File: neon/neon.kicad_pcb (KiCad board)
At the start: 2 copper layers, 60 x 50 mm, 46 parts, among them J1 V3V3-VIO, J2 V3V3-GND, J3 V3V3-GND, J4 V3V3-GND, J5 VBUS-VCC, Q1 BC807, Q2 BC807, Q3 BC807, Q4 BC807, Q5 BC807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

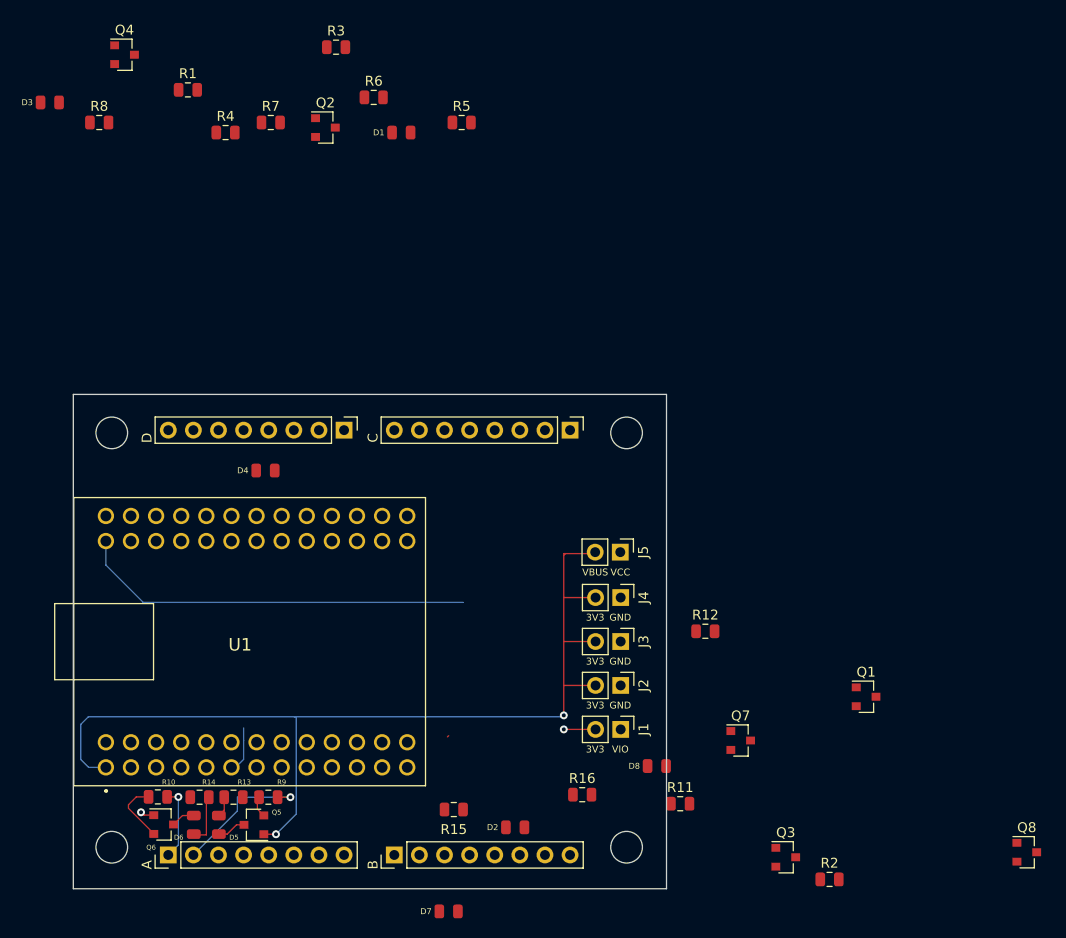
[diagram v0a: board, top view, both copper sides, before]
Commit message: Version with shift register - schematic
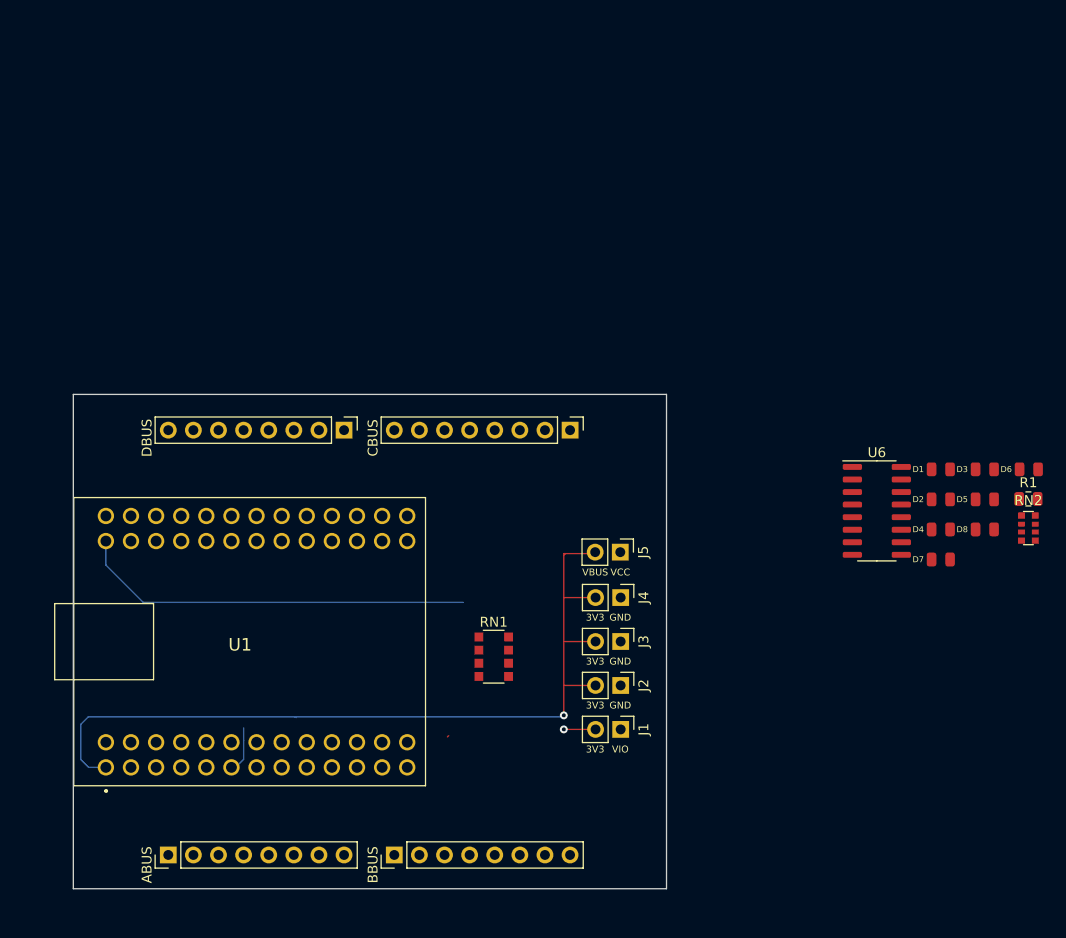
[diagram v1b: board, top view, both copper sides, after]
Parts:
- removed Q1, Q2, Q3, Q4, Q5, Q6, Q7, Q8: BC807, Package_TO_SOT_SMD:SOT-23
- removed R10, R11, R12, R5, R6, R7, R8, R9: 10k, Resistor_SMD:R_0805_2012Metric
- removed R13, R14, R15, R16, R2, R3, R4: 330, Resistor_SMD:R_0805_2012Metric
- removed REF** (x4): MountingHole_3.2mm_M3, MountingHole:MountingHole_3.2mm_M3
- added RN1: 330, Resistor_SMD:R_Array_Convex_4x1206, F.Cu at (158.0, 106.5)
- added RN2: 330, Resistor_SMD:R_Array_Convex_4x0612, F.Cu at (212.1, 93.5)
- added U6: 74HC595, Package_SO:SOIC-16_3.9x9.9mm_P1.27mm, F.Cu at (196.8, 91.7)
- R1: value 330 -> 10k
- U2: value A -> ABUS
- U3: value B -> BBUS
- U4: value C -> CBUS
- U5: value D -> DBUS
- moved D3 101.6 mm to (207.7, 87.5)
- moved R1 94.5 mm to (212.1, 90.5)
- moved D6 91.8 mm to (212.1, 87.5), turned to 0 degrees
- moved D5 84.2 mm to (207.7, 90.5), turned to 0 degrees
- moved D4 68.6 mm to (203.2, 93.6)
- moved D1 64.3 mm to (203.2, 87.5)
- moved D7 61.2 mm to (203.2, 96.6)
- moved D2 54.3 mm to (203.2, 90.5)
- moved D8 40.9 mm to (207.7, 93.6)
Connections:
- D1 pad 1: Net-(D1-Pad1) -> GND
- D2 pad 1: Net-(D2-Pad1) -> GND
- D3 pad 1: Net-(D3-Pad1) -> GND
- D4 pad 1: Net-(D4-Pad1) -> GND
- D5 pad 1: Net-(D5-Pad1) -> GND
- D6 pad 1: Net-(D6-Pad1) -> GND
- D7 pad 1: Net-(D7-Pad1) -> GND
- D8 pad 1: Net-(D8-Pad1) -> GND
- R1 pad 1: Net-(D1-Pad1) -> /FT4232H.sch/PWREN
- R1 pad 2: GND -> /FT4232H.sch/VIO
- U1 pad 29: Net-(U1-Pad29) -> /FT4232H.sch/CS
- U1 pad 30: Net-(U1-Pad30) -> /FT4232H.sch/DATA
- U1 pad 42: Net-(U1-Pad42) -> /FT4232H.sch/CLK
- U1 pad 43: Net-(U1-Pad43) -> /FT4232H.sch/PWREN
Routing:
- net V3V3: track 100.2 -> 84.9 mm, vias 4 -> 2
- net /FT4232H.sch/AD1: track 14.4 -> 0.00 mm, vias 1 -> 0
- net /FT4232H.sch/AD0: track 7.44 -> 0.00 mm, vias 1 -> 0
- net Net-(Q6-Pad2): track 6.60 -> 0.00 mm
- net Net-(D6-Pad1): track 5.16 -> 0.00 mm
- net Net-(D5-Pad2): track 3.04 -> 0.00 mm
- net Net-(D6-Pad2): track 2.42 -> 0.00 mm
- net Net-(D5-Pad1): track 2.19 -> 0.00 mm
- net Net-(Q5-Pad2): track 2.11 -> 0.00 mm

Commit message: Assign LEDs on pcb
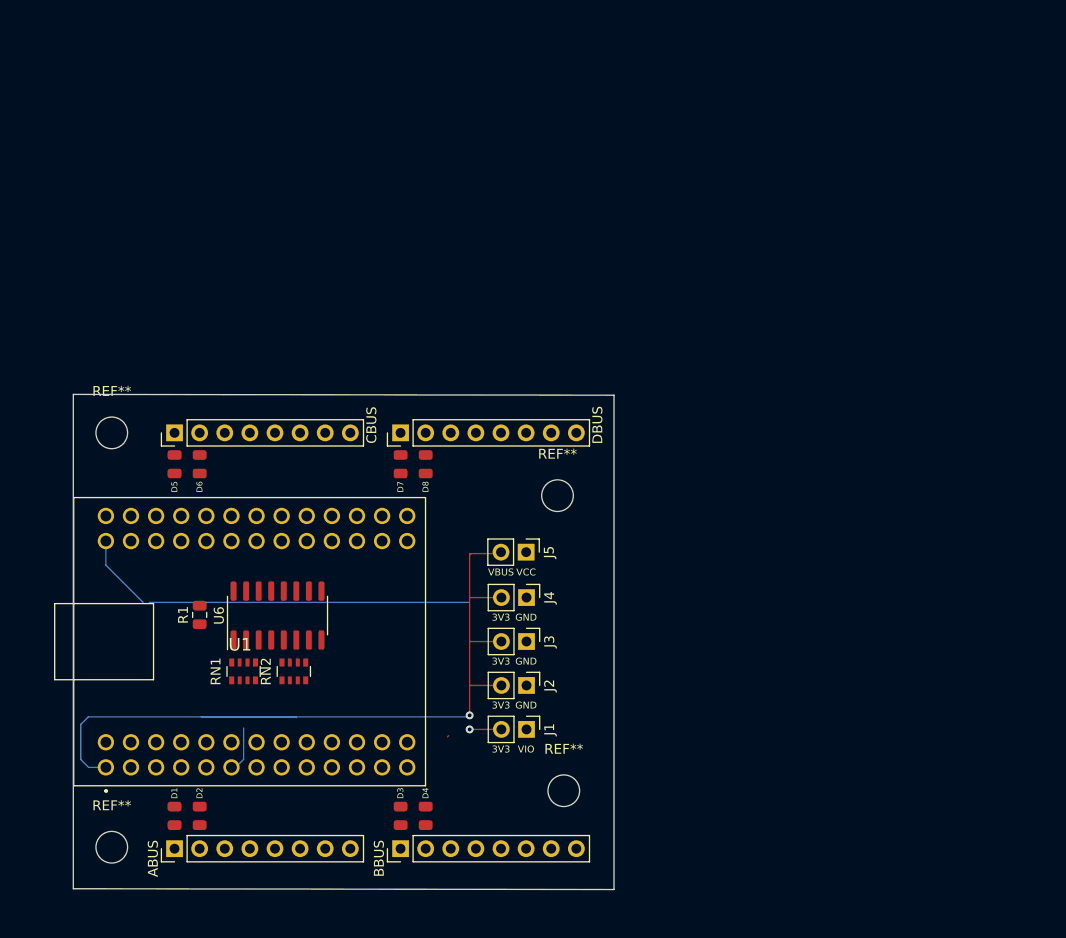
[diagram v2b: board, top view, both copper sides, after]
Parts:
- added REF**: MountingHole_3.2mm_M3, MountingHole:MountingHole_3.2mm_M3, F.Cu at (165.1, 120.0)
- added REF**: MountingHole_3.2mm_M3, MountingHole:MountingHole_3.2mm_M3, F.Cu at (164.5, 90.2)
- added REF**: MountingHole_3.2mm_M3, MountingHole:MountingHole_3.2mm_M3, F.Cu at (119.4, 125.7)
- added REF**: MountingHole_3.2mm_M3, MountingHole:MountingHole_3.2mm_M3, F.Cu at (119.4, 83.8)
- RN1: footprint Resistor_SMD:R_Array_Convex_4x1206 -> Resistor_SMD:R_Array_Convex_4x0603
- RN2: footprint Resistor_SMD:R_Array_Convex_4x0612 -> Resistor_SMD:R_Array_Convex_4x0603
- moved D1 85.1 mm to (125.7, 122.6), turned to 270 degrees
- moved R1 84.6 mm to (128.3, 102.2), turned to 90 degrees
- moved D6 83.9 mm to (128.3, 87.0), turned to 90 degrees
- moved D5 82.0 mm to (125.7, 87.0), turned to 90 degrees
- moved D2 81.5 mm to (128.3, 122.6), turned to 270 degrees
- moved RN2 75.7 mm to (137.8, 108.0), turned to 90 degrees
- moved D3 68.7 mm to (148.6, 122.6), turned to 270 degrees
- moved U6 61.5 mm to (136.1, 102.3), turned to 90 degrees
- moved D4 59.6 mm to (151.1, 122.6), turned to 270 degrees
- moved D8 56.9 mm to (151.1, 87.0), turned to 90 degrees
- moved D7 55.5 mm to (148.6, 87.0), turned to 90 degrees
- moved U4 40.0 mm to (125.7, 83.8), turned to 90 degrees
- moved RN1 25.3 mm to (132.7, 108.0), turned to 90 degrees
- moved J1 9.53 mm to (161.3, 113.8)
- moved J2 9.53 mm to (161.3, 109.4)
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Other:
- board size 60 x 50 mm -> 54.7 x 50.1 mm

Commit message: A BUS
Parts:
- turned D1 to 90 degrees
- turned D2 to 90 degrees
- turned D3 to 90 degrees
- turned D4 to 90 degrees
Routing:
- net /FT4232H.sch/VBUS: track 43.5 -> 0.18 mm
- net Net-(D2-Pad2): track 0.00 -> 34.4 mm
- net Net-(D1-Pad2): track 0.00 -> 33.0 mm
- net Net-(D3-Pad2): track 0.00 -> 30.9 mm
- net Net-(D4-Pad2): track 0.00 -> 29.2 mm
- net Net-(RN1-Pad8): track 0.00 -> 18.4 mm, vias 0 -> 2
- net /FT4232H.sch/AD6: track 0.00 -> 13.7 mm
- net /FT4232H.sch/AD4: track 0.00 -> 12.6 mm
- net /FT4232H.sch/AD3: track 0.00 -> 12.6 mm
- net /FT4232H.sch/AD7: track 0.00 -> 11.9 mm
- net /FT4232H.sch/AD1: track 0.00 -> 11.8 mm
- net /FT4232H.sch/AD5: track 0.00 -> 10.0 mm
- net /FT4232H.sch/AD2: track 0.00 -> 9.00 mm
- net /FT4232H.sch/AD0: track 0.00 -> 8.50 mm
- net GND: track 0.00 -> 4.62 mm, vias 0 -> 1
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
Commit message: Texts ideas
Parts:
- U2: value ABUS -> A; footprint Connector_PinHeader_2.54mm:PinHeader_1x08_P2.54mm_Vertical -> neon_footprints:PinHeader_1x08_P2.54mm_Vertical
- U3: value BBUS -> B; footprint Connector_PinHeader_2.54mm:PinHeader_1x08_P2.54mm_Vertical -> neon_footprints:PinHeader_1x08_P2.54mm_Vertical
- U4, U5: footprint Connector_PinHeader_2.54mm:PinHeader_1x08_P2.54mm_Vertical -> neon_footprints:PinHeader_1x08_P2.54mm_Vertical
- moved D4 1.28 mm to (151.7, 121.4), turned to 0 degrees
- moved D3 1.18 mm to (148.3, 121.4), turned to 180 degrees
- moved D1 0.51 mm to (125.7, 122.0)
- moved D2 0.51 mm to (128.3, 122.0)
- moved U2 0.51 mm to (125.7, 125.4)
- moved U3 0.51 mm to (148.6, 125.4)
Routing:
- net Net-(D4-Pad2): track 29.2 -> 21.4 mm
- net GND: track 4.62 -> 12.4 mm
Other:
- board size 54.7 x 50.1 mm -> 54.7 x 50 mm
- board text added: "0"
- board text added: "1"
- board text added: "2"
- board text added: "3"
- board text added: "CS"
- board text added: "CTS"
- board text added: "DCD"
- board text added: "DSR"
- board text added: "DTR"
- board text added: "GPIO"
- board text added: "MISO"
- board text added: "MOSI"
- board text added: "RI"
- board text added: "RTS"
- board text added: "RX"
- board text added: "SCK"
- board text added: "TCK"
- board text added: "TDI"
- board text added: "TDO"
- board text added: "TMS"
- board text added: "TX"

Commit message: More labels
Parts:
- U5: value DBUS -> D
- moved D7 1.27 mm to (148.6, 88.3)
- moved D8 1.27 mm to (151.1, 88.3)
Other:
- board text added: "4"
- board text added: "5"
- board text added: "6"
- board text added: "7"
- board text added: "GPIO0"
- board text added: "GPIO1"
- board text added: "GPIO2"
- board text added: "GPIO3"
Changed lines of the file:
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@@
   (general
     (thickness 1.6)
-    (drawings 65)
+    (drawings 121)
     (tracks 109)
     (zones 0)
@@
       (effects (font (size 1 1) (thickness 0.15)))
     )
-    (fp_text value DBUS (at -0.1054 -2.159 90) (layer F.SilkS)
-      (effects (font (size 1 1) (thickness 0.15)))
-    )
-    (fp_text user %R (at -1.175 9.634 180) (layer F.Fab)
+    (fp_text value D (at -0.1054 -2.159 90) (layer F.SilkS)
+      (effects (font (size 1 1) (thickness 0.15)))
+    )
+    (fp_text user %R (at 0 19.812 180) (layer F.Fab)
       (effects (font (size 1 1) (thickness 0.15)))
     )
@@
   )
   (module neon_footprints:LED_0805_2012Metric (layer F.Cu)
-    (at 151.13 86.995 90)
+    (at 151.13 88.265 90)
     (descr "LED SMD 0805 (2012 Metric), square (rectangular) end terminal, IPC_7351 nominal, (Body size source: https://docs.google.com/spreadsheets/d/1BsfQQcO9C6DZCsRaXUlFlo91Tg2WpOkGARC1WS5S8t0/edit?usp=sharing), generated with kicad-footprint-generator")
     (tags diode)
@@
   )
   (module neon_footprints:LED_0805_2012Metric (layer F.Cu)
-    (at 148.59 86.995 90)
+    (at 148.59 88.265 90)
     (descr "LED SMD 0805 (2012 Metric), square (rectangular) end terminal, IPC_7351 nominal, (Body size source: https://docs.google.com/spreadsheets/d/1BsfQQcO9C6DZCsRaXUlFlo91Tg2WpOkGARC1WS5S8t0/edit?usp=sharing), generated with kicad-footprint-generator")
     (tags diode)
@@
     )
   )
+  (gr_text TMS (at 132.842 79.756 90) (layer F.SilkS)
+    (effects (font (size 0.7112 0.7112) (thickness 0.175)) (justify left))
+  )
+  (gr_text TDO (at 130.302 79.756 90) (layer F.SilkS)
+    (effects (font (size 0.7112 0.7112) (thickness 0.175)) (justify left))
+  )
+  (gr_text GPIO1 (at 138.938 82.296 90) (layer F.SilkS)
+    (effects (font (size 0.7112 0.7112) (thickness 0.175)) (justify left))
+  )
+  (gr_text GPIO2 (at 141.478 82.296 90) (layer F.SilkS)
+    (effects (font (size 0.7112 0.7112) (thickness 0.175)) (justify left))
+  )
+  (gr_text TDI (at 127.762 79.756 90) (layer F.SilkS)
+    (effects (font (size 0.7112 0.7112) (thickness 0.175)) (justify left))
+  )
+  (gr_text "GPIO3\n" (at 144.018 82.296 90) (layer F.SilkS)
+    (effects (font (size 0.7112 0.7112) (thickness 0.175)) (justify left))
+  )
+  (gr_text MISO (at 131.318 79.756 90) (layer F.SilkS)
+    (effects (font (size 0.7112 0.7112) (thickness 0.175)) (justify left))
+  )
+  (gr_text CS (at 133.858 79.756 90) (layer F.SilkS)
+    (effects (font (size 0.7112 0.7112) (thickness 0.175)) (justify left))
+  )
+  (gr_text TCK (at 125.222 79.756 90) (layer F.SilkS)
+    (effects (font (size 0.7112 0.7112) (thickness 0.175)) (justify left))
+  )
+  (gr_text MOSI (at 128.778 79.756 90) (layer F.SilkS)
+    (effects (font (size 0.7112 0.7112) (thickness 0.175)) (justify left))
+  )
+  (gr_text SCK (at 126.238 79.756 90) (layer F.SilkS)
+    (effects (font (size 0.7112 0.7112) (thickness 0.175)) (justify left))
+  )
+  (gr_text RI (at 143.002 82.296 90) (layer F.SilkS)
+    (effects (font (size 0.7112 0.7112) (thickness 0.175)) (justify left))
+  )
+  (gr_text GPIO0 (at 136.398 82.296 90) (layer F.SilkS)
+    (effects (font (size 0.7112 0.7112) (thickness 0.175)) (justify left))
+  )
+  (gr_text 4 (at 135.89 85.09 90) (layer F.SilkS)
+    (effects (font (size 0.9144 0.9144) (thickness 0.175)) (justify right))
+  )
+  (gr_text 3 (at 133.35 85.09 90) (layer F.SilkS)
+    (effects (font (size 0.9144 0.9144) (thickness 0.175)) (justify right))
+  )
+  (gr_text 2 (at 130.81 85.09 90) (layer F.SilkS)
+    (effects (font (size 0.9144 0.9144) (thickness 0.175)) (justify right))
+  )
+  (gr_text 0 (at 125.73 85.09 90) (layer F.SilkS)
+    (effects (font (size 0.9144 0.9144) (thickness 0.175)) (justify right))
+  )
+  (gr_text RX (at 128.27 82.296 90) (layer F.SilkS)
+    (effects (font (size 0.8128 0.8128) (thickness 0.175)) (justify left))
+  )
+  (gr_text 6 (at 140.97 85.09 90) (layer F.SilkS)
+    (effects (font (size 0.9144 0.9144) (thickness 0.175)) (justify right))
+  )
+  (gr_text 7 (at 143.51 85.09 90) (layer F.SilkS)
+    (effects (font (size 0.9144 0.9144) (thickness 0.175)) (justify right))
+  )
+  (gr_text 1 (at 128.27 85.09 90) (layer F.SilkS)
+    (effects (font (size 0.9144 0.9144) (thickness 0.175)) (justify right))
+  )
+  (gr_text 5 (at 138.43 85.09 90) (layer F.SilkS)
+    (effects (font (size 0.9144 0.9144) (thickness 0.175)) (justify right))
+  )
+  (gr_text DCD (at 140.462 82.296 90) (layer F.SilkS)
+    (effects (font (size 0.7112 0.7112) (thickness 0.175)) (justify left))
+  )
+  (gr_text TX (at 125.73 82.296 90) (layer F.SilkS)
+    (effects (font (size 0.8128 0.8128) (thickness 0.175)) (justify left))
+  )
+  (gr_text RTS (at 130.81 82.296 90) (layer F.SilkS)
+    (effects (font (size 0.8128 0.8128) (thickness 0.175)) (justify left))
+  )
+  (gr_text DSR (at 137.922 82.296 90) (layer F.SilkS)
+    (effects (font (size 0.7112 0.7112) (thickness 0.175)) (justify left))
+  )
+  (gr_text "CTS\n" (at 133.35 82.296 90) (layer F.SilkS)
+    (effects (font (size 0.8128 0.8128) (thickness 0.175)) (justify left))
+  )
+  (gr_text DTR (at 135.382 82.296 90) (layer F.SilkS)
+    (effects (font (size 0.7112 0.7112) (thickness 0.175)) (justify left))
+  )
+  (gr_text CS (at 156.21 77.216 90) (layer F.SilkS)
+    (effects (font (size 0.7112 0.7112) (thickness 0.175)) (justify left))
+  )
+  (gr_text MISO (at 153.67 77.216 90) (layer F.SilkS)
+    (effects (font (size 0.7112 0.7112) (thickness 0.175)) (justify left))
+  )
+  (gr_text MOSI (at 151.13 77.216 90) (layer F.SilkS)
+    (effects (font (size 0.7112 0.7112) (thickness 0.175)) (justify left))
+  )
+  (gr_text SCK (at 148.59 77.216 90) (layer F.SilkS)
+    (effects (font (size 0.7112 0.7112) (thickness 0.175)) (justify left))
+  )
+  (gr_text "GPIO3\n" (at 166.37 79.756 90) (layer F.SilkS)
+    (effects (font (size 0.7112 0.7112) (thickness 0.175)) (justify left))
+  )
+  (gr_text TDI (at 151.13 79.756 90) (layer F.SilkS)
+    (effects (font (size 0.7112 0.7112) (thickness 0.175)) (justify left))
+  )
+  (gr_text GPIO2 (at 163.83 79.756 90) (layer F.SilkS)
+    (effects (font (size 0.7112 0.7112) (thickness 0.175)) (justify left))
+  )
+  (gr_text TCK (at 148.59 79.756 90) (layer F.SilkS)
+    (effects (font (size 0.7112 0.7112) (thickness 0.175)) (justify left))
+  )
+  (gr_text TDO (at 153.67 79.756 90) (layer F.SilkS)
+    (effects (font (size 0.7112 0.7112) (thickness 0.175)) (justify left))
+  )
+  (gr_text GPIO1 (at 161.29 79.756 90) (layer F.SilkS)
+    (effects (font (size 0.7112 0.7112) (thickness 0.175)) (justify left))
+  )
+  (gr_text TMS (at 156.21 79.756 90) (layer F.SilkS)
+    (effects (font (size 0.7112 0.7112) (thickness 0.175)) (justify left))
+  )
+  (gr_text GPIO0 (at 158.75 79.756 90) (layer F.SilkS)
+    (effects (font (size 0.7112 0.7112) (thickness 0.175)) (justify left))
+  )
+  (gr_text 7 (at 166.37 85.09 90) (layer F.SilkS)
+    (effects (font (size 0.7112 0.7112) (thickness 0.175)) (justify right))
+  )
+  (gr_text 6 (at 163.83 85.09 90) (layer F.SilkS)
+    (effects (font (size 0.7112 0.7112) (thickness 0.175)) (justify right))
+  )
+  (gr_text 5 (at 161.29 85.09 90) (layer F.SilkS)
+    (effects (font (size 0.7112 0.7112) (thickness 0.175)) (justify right))
+  )
+  (gr_text 4 (at 158.75 85.09 90) (layer F.SilkS)
+    (effects (font (size 0.7112 0.7112) (thickness 0.175)) (justify right))
+  )
+  (gr_text 3 (at 156.21 85.09 90) (layer F.SilkS)
+    (effects (font (size 0.7112 0.7112) (thickness 0.175)) (justify right))
+  )
+  (gr_text 2 (at 153.67 85.09 90) (layer F.SilkS)
+    (effects (font (size 0.7112 0.7112) (thickness 0.175)) (justify right))
+  )
+  (gr_text 1 (at 151.13 85.09 90) (layer F.SilkS)
+    (effects (font (size 0.7112 0.7112) (thickness 0.175)) (justify right))
+  )
+  (gr_text 0 (at 148.59 85.09 90) (layer F.SilkS)
+    (effects (font (size 0.7112 0.7112) (thickness 0.175)) (justify right))
+  )
+  (gr_text RX (at 151.13 82.296 90) (layer F.SilkS)
+    (effects (font (size 0.7112 0.7112) (thickness 0.175)) (justify left))
+  )
+  (gr_text RI (at 166.37 82.296 90) (layer F.SilkS)
+    (effects (font (size 0.7112 0.7112) (thickness 0.175)) (justify left))
+  )
+  (gr_text DCD (at 163.83 82.296 90) (layer F.SilkS)
+    (effects (font (size 0.7112 0.7112) (thickness 0.175)) (justify left))
+  )
+  (gr_text DSR (at 161.29 82.296 90) (layer F.SilkS)
+    (effects (font (size 0.7112 0.7112) (thickness 0.175)) (justify left))
+  )
+  (gr_text "CTS\n" (at 156.21 82.296 90) (layer F.SilkS)
+    (effects (font (size 0.7112 0.7112) (thickness 0.175)) (justify left))
+  )
+  (gr_text DTR (at 158.75 82.296 90) (layer F.SilkS)
+    (effects (font (size 0.7112 0.7112) (thickness 0.175)) (justify left))
+  )
+  (gr_text RTS (at 153.67 82.296 90) (layer F.SilkS)
+    (effects (font (size 0.7112 0.7112) (thickness 0.175)) (justify left))
+  )
+  (gr_text TX (at 148.59 82.296 90) (layer F.SilkS)
+    (effects (font (size 0.7112 0.7112) (thickness 0.175)) (justify left))
+  )
   (gr_line (start 170.18 129.93) (end 115.49 129.93) (layer Edge.Cuts) (width 0.05))

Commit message: Labels four versions
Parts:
- added U4: C, neon_footprints:PinHeader_1x08_P2.54mm_Vertical, F.Cu at (125.7, 85.1)
- U4: value CBUS -> C
- moved J2 7.01 mm to (168.3, 108.7)
- moved J4 7.01 mm to (168.3, 99.8)
- moved J5 7.01 mm to (168.3, 95.2)
- moved J1 7.01 mm to (168.3, 113.2)
- moved J3 7.01 mm to (168.3, 104.3)
- moved D5 2.01 mm to (125.1, 88.9), turned to 180 degrees
- moved D6 2.01 mm to (128.9, 88.9), turned to 180 degrees
- moved U4 1.90 mm to (125.7, 81.9)
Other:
- board size 54.7 x 50 mm -> 54.7 x 55 mm
